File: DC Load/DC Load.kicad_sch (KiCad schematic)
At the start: 11 parts, among them J1 VSENSE, J2 LOAD_POS, J3 LOAD_NEG, U8 OPA2182

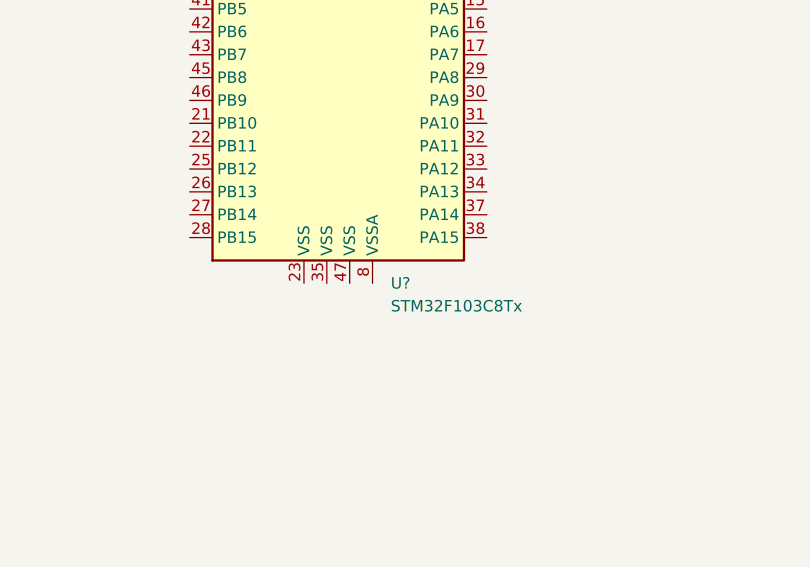
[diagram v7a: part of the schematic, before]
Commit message: Swap DAC to MAX5217
Allows use of 2.048v ref with 3.3V VDD
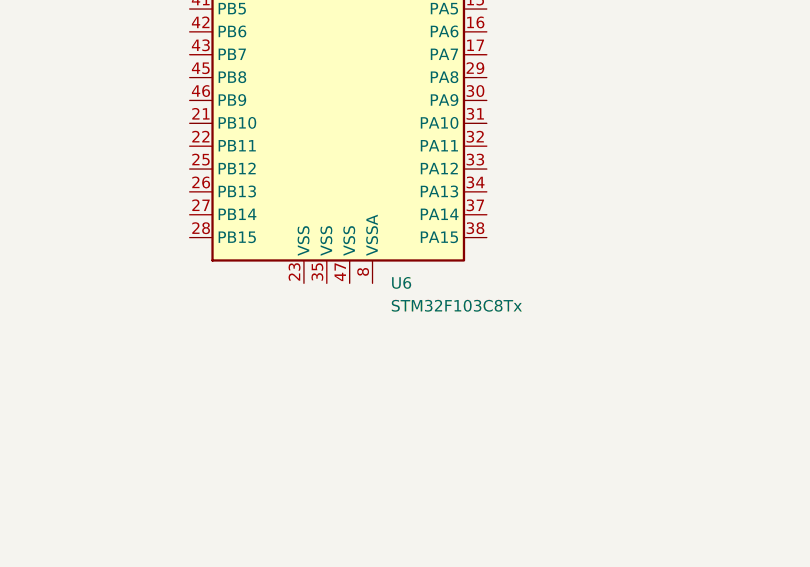
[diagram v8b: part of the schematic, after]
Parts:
- gave numbers to parts that had none: 1
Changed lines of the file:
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@@
   (symbol (lib_id "MCU_ST_STM32F1:STM32F103C8Tx") (at 114.3 69.85 0) (unit 1)
     (in_bom yes) (on_board yes) (fields_autoplaced)
-    (property "Reference" "U?" (id 0) (at 118.8594 107.95 0)
+    (property "Reference" "U6" (id 0) (at 118.8594 107.95 0)
       (effects (font (size 1.27 1.27)) (justify left))
     )
@@
       (reference "#PWR010") (unit 1) (value "GND") (footprint "")
     )
-    (path "/dfd5aec5-c760-49fb-a2c5-6076cb755a00/b8e558a9-5f4a-45a5-aa1c-03f01c511d9e"
-      (reference "#PWR011") (unit 1) (value "+2.048V") (footprint "")
+    (path "/dfd5aec5-c760-49fb-a2c5-6076cb755a00/b7732f89-4925-4bee-8cb3-3d1d66323d48"
+      (reference "#PWR011") (unit 1) (value "+5V") (footprint "")
+    )
+    (path "/dfd5aec5-c760-49fb-a2c5-6076cb755a00/bc2ccd60-cc8e-4831-b51c-e30aa927e79a"
+      (reference "#PWR012") (unit 1) (value "GND") (footprint "")
     )
     (path "/dfd5aec5-c760-49fb-a2c5-6076cb755a00/f575cc6b-b6f6-44d5-a9fa-e8868654eb82"
@@
       (reference "#PWR027") (unit 1) (value "GND") (footprint "")
     )
-    (path "/dfd5aec5-c760-49fb-a2c5-6076cb755a00/2d868b43-5c88-46e1-b4bf-ebd6a113b601"
-      (reference "#PWR028") (unit 1) (value "+5V") (footprint "")
-    )
-    (path "/dfd5aec5-c760-49fb-a2c5-6076cb755a00/fe5d494f-1cd3-468d-830f-faf9fa453e77"
-      (reference "#PWR029") (unit 1) (value "GND") (footprint "")
+    (path "/dfd5aec5-c760-49fb-a2c5-6076cb755a00/a5c13df8-376f-42ac-bdf1-e84e19d548ab"
+      (reference "#PWR028") (unit 1) (value "+2.048V") (footprint "")
     )
     (path "/dfd5aec5-c760-49fb-a2c5-6076cb755a00/aad6e91b-812e-485c-a780-1e6007756cf8"
       (reference "#PWR0101") (unit 1) (value "+5V") (footprint "")
     )
-    (path "/dfd5aec5-c760-49fb-a2c5-6076cb755a00/b7732f89-4925-4bee-8cb3-3d1d66323d48"
-      (reference "#PWR?") (unit 1) (value "+5V") (footprint "")
-    )
     (path "/16aec46b-6a38-4237-b970-7429d50e0368"
       (reference "A1") (unit 1) (value "Arduino_Nano_v3.x") (footprint "Module:Arduino_Nano")
@@
       (reference "C11") (unit 1) (value "10uF") (footprint "")
     )
-    (path "/dfd5aec5-c760-49fb-a2c5-6076cb755a00/bf65b4f8-d772-4e15-8de7-3a15074c730f"
-      (reference "C12") (unit 1) (value "0.1uF") (footprint "")
-    )
     (path "/dfd5aec5-c760-49fb-a2c5-6076cb755a00/8ae9dc19-cf40-42a2-a0fc-a6f648feb868"
       (reference "C13") (unit 1) (value "0.1uF") (footprint "")
@@
       (reference "IC2") (unit 1) (value "LTC1046CS8#PBF") (footprint "SOIC127P599X175-8N")
     )
-    (path "/dfd5aec5-c760-49fb-a2c5-6076cb755a00/3c644894-f2cb-401d-a6fe-03d7eea20c69"
-      (reference "IC3") (unit 1) (value "DAC80501MDGST") (footprint "SOP50P490X110-10N")
-    )
     (path "/51e2b8b9-06ec-4d7b-b206-36f4a8777eae"
       (reference "J1") (unit 1) (value "VSENSE") (footprint "")
@@
       (reference "R24") (unit 1) (value "0R1 1% 2W") (footprint "")
     )
-    (path "/dfd5aec5-c760-49fb-a2c5-6076cb755a00/0001a2e9-b4a8-45b2-9215-dd269d8df025"
-      (reference "R25") (unit 1) (value "10K") (footprint "")
-    )
     (path "/ee92d22e-f0a9-4e83-8faa-8b8475bbee5f/b08878ec-f22d-416b-8d92-62f5f678b00d"
       (reference "R26") (unit 1) (value "470K") (footprint "")
@@
       (reference "R44") (unit 1) (value "10K") (footprint "")
     )
-    (path "/dfd5aec5-c760-49fb-a2c5-6076cb755a00/4822bfb9-9c44-4689-bc37-7cc88297a6ac"
-      (reference "R45") (unit 1) (value "10K") (footprint "")
-    )
     (path "/dfd5aec5-c760-49fb-a2c5-6076cb755a00/a2974e2e-5439-4050-a37e-28b2d5a035b2"
       (reference "R46") (unit 1) (value "100") (footprint "")
@@
       (reference "U5") (unit 1) (value "REF5020AID") (footprint "Package_SO:SOIC-8_3.9x4.9mm_P1.27mm")
     )
+    (path "/fe9fcdce-5b99-4eca-bfaa-591ba3bc2fef"
+      (reference "U6") (unit 1) (value "STM32F103C8Tx") (footprint "Package_QFP:LQFP-48_7x7mm_P0.5mm")
+    )
     (path "/dfd5aec5-c760-49fb-a2c5-6076cb755a00/e805cec0-25c2-4590-9bc5-079241905cd3"
       (reference "U7") (unit 1) (value "MCP3426") (footprint "")
@@
       (reference "U10") (unit 1) (value "MC7805BD2TR4G") (footprint "Package_TO_SOT_SMD:TO-263-3_TabPin2")
     )
-    (path "/fe9fcdce-5b99-4eca-bfaa-591ba3bc2fef"
-      (reference "U?") (unit 1) (value "STM32F103C8Tx") (footprint "Package_QFP:LQFP-48_7x7mm_P0.5mm")
+    (path "/dfd5aec5-c760-49fb-a2c5-6076cb755a00/96a0782b-64d0-499a-a826-47e1d2678216"
+      (reference "U11") (unit 1) (value "MAX5217") (footprint "Package_SO:MSOP-8_3x3mm_P0.65mm")
     )
   )
